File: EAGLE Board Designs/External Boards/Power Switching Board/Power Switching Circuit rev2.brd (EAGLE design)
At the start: 93.6 x 68.1 mm, 64 parts, among them J1 CONNECTOR-3_, J2 CONNECTOR-4_SOURIAU_, J3 CONNECTOR-4_SOURIAU_, K1 J115F11A6*, Q1 TRANSISTOR_N_MOS_2-7K1S_TK100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, Q2 TRANSISTOR_N_MOS_2-7K1S_TK100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, Q3 TRANSISTOR_N_MOS_2-7K1S_TK100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, Q4 TRANSISTOR_N_MOS_2-7K1S_TK100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, U1 LTC4421

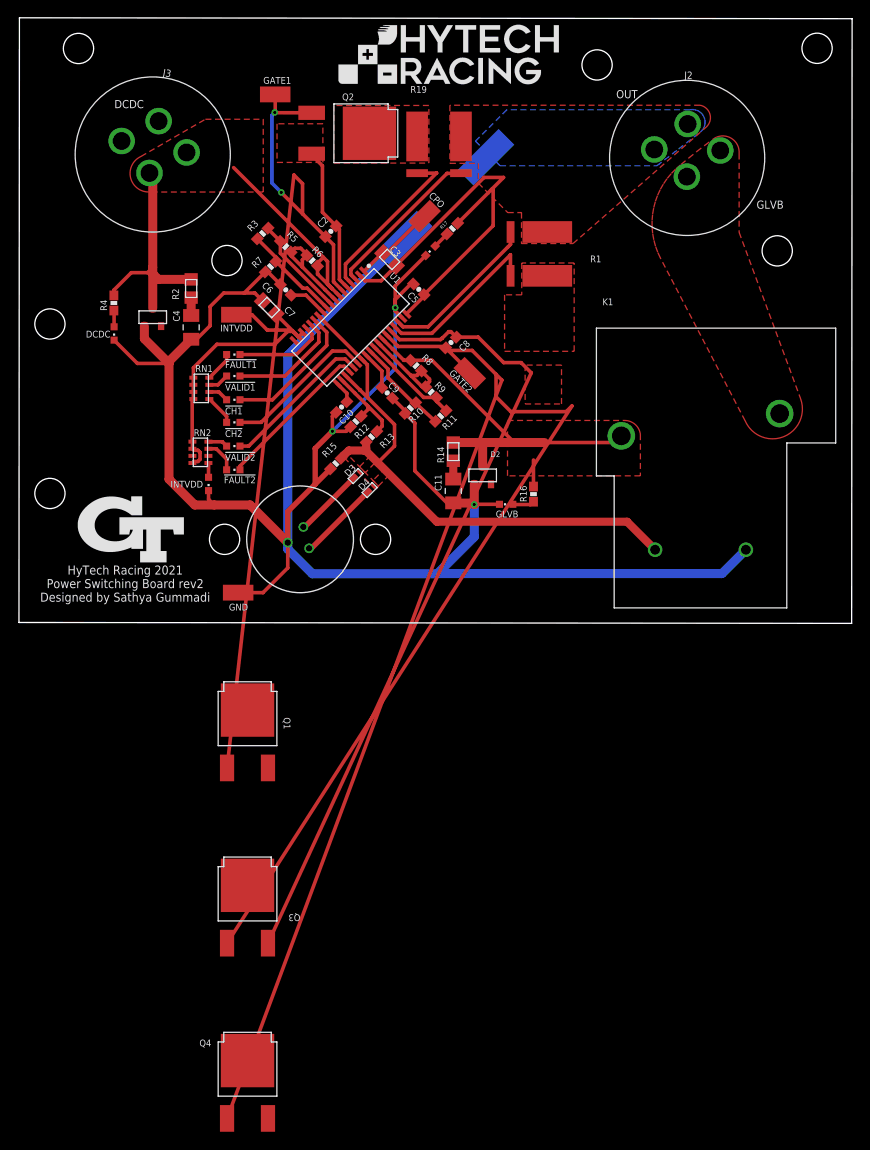
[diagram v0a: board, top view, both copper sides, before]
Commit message: Revert "Replaced mosfets with new device in new library"
This reverts commit 47685a596586f3a57bfaa4732962c561ce9df098.
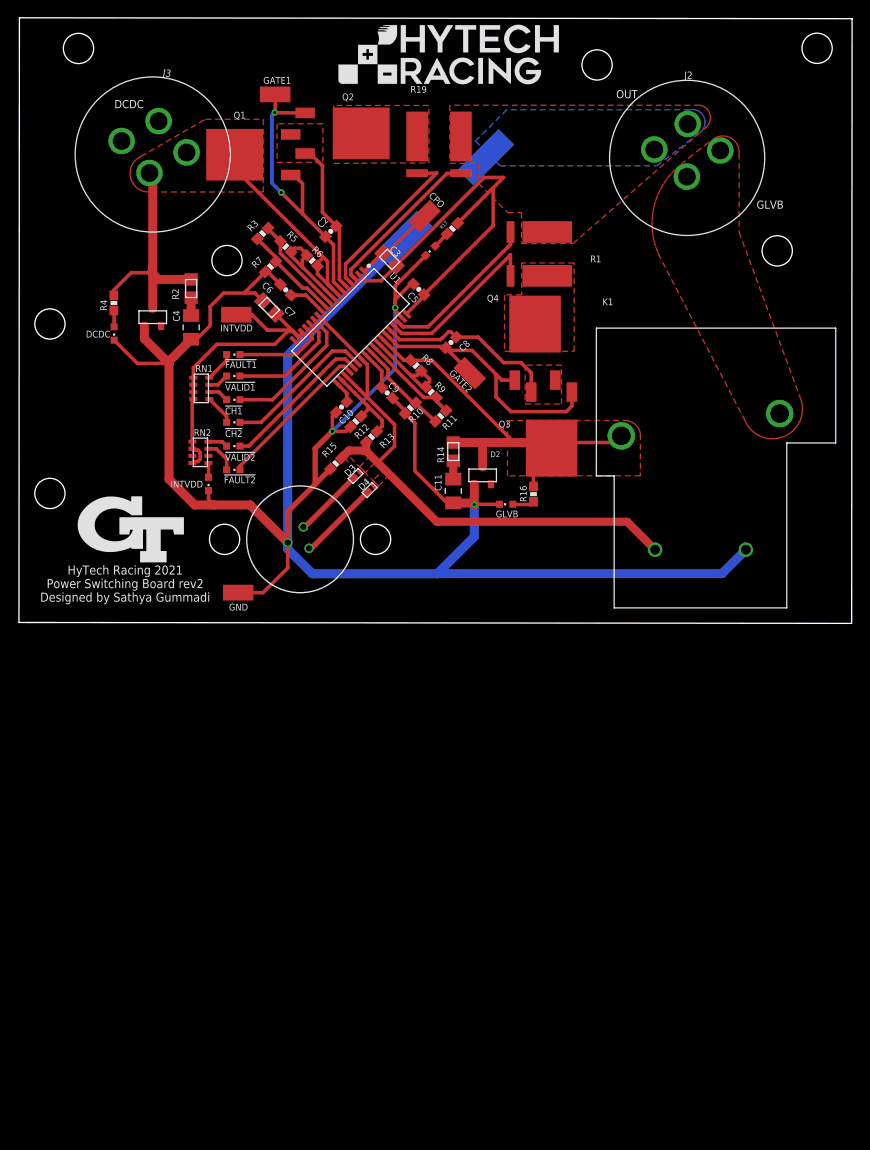
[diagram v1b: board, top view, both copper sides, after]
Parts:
- Q1, Q2, Q3, Q4: value TRANSISTOR_N_MOS_2-7K1S_TK100S04N1L,LQ -> TK100S04N1L; device HyTechDevices:DPAK(2-7K1S) -> HyTechDevices:TO-252-3
- moved Q4 89.7 mm to (30.0, 3.00)
- moved Q1 65.4 mm to (-1.68, 24.1), turned to 90 degrees
- moved Q3 64.1 mm to (31.9, -6.81), turned to 180 degrees
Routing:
- net GATE2: track 191.5 -> 34.2 mm
- net SOURCE2: track 89.2 -> 20.8 mm
- net GATE1: track 101.8 -> 34.4 mm
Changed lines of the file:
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@@
 <attribute name="RESISTANCE" value="0.0013" x="28.1178" y="11.938" size="1.778" layer="27" rot="R180" display="off"/>
 </element>
-<element name="Q1" library="HyTechDevices" package="DPAK(2-7K1S)" value="TRANSISTOR_N_MOS_2-7K1S_TK100S04N1L,LQ" x="-2.3" y="-41.3206" smashed="yes">
-<attribute name="DKPN" value="TK100S04N1LLQ" x="-2.3" y="-41.3206" size="1.778" layer="27" display="off"/>
-<attribute name="MANUFACTURER" value="Toshiba Semiconductor and Storage" x="-2.3" y="-41.3206" size="1.778" layer="27" display="off"/>
-<attribute name="MOPN" value="757-TK100S04N1LLQ" x="-2.3" y="-41.3206" size="1.778" layer="27" display="off"/>
-<attribute name="MPN" value="TK100S04N1L,LQ" x="-2.3" y="-41.3206" size="1.778" layer="27" display="off"/>
-<attribute name="NAME" x="1.764" y="-39.1362" size="0.762" layer="25" ratio="6" rot="SR270"/>
+<element name="Q1" library="HyTechDevices" package="TO-252-3" value="TK100S04N1L" x="-1.6764" y="24.1046" smashed="yes" rot="R90">
+<attribute name="MPN" value="TK100S04N1L,LQ" x="-1.6764" y="24.1046" size="1.778" layer="27" rot="R90" display="off"/>
+<attribute name="NAME" x="-3.8608" y="28.1686" size="0.762" layer="25" ratio="6" rot="SR0"/>
 </element>
-<element name="Q2" library="HyTechDevices" package="DPAK(2-7K1S)" value="TRANSISTOR_N_MOS_2-7K1S_TK100S04N1L,LQ" x="8.4074" y="26.5176" smashed="yes" rot="R270">
-<attribute name="DKPN" value="TK100S04N1LLQ" x="8.4074" y="26.5176" size="1.778" layer="27" rot="R270" display="off"/>
-<attribute name="MANUFACTURER" value="Toshiba Semiconductor and Storage" x="8.4074" y="26.5176" size="1.778" layer="27" rot="R270" display="off"/>
-<attribute name="MOPN" value="757-TK100S04N1LLQ" x="8.4074" y="26.5176" size="1.778" layer="27" rot="R270" display="off"/>
+<element name="Q2" library="HyTechDevices" package="TO-252-3" value="TK100S04N1L" x="8.4074" y="26.5176" smashed="yes" rot="R270">
 <attribute name="MPN" value="TK100S04N1L,LQ" x="8.4074" y="26.5176" size="1.778" layer="27" rot="R270" display="off"/>
 <attribute name="NAME" x="8.3312" y="30.226" size="0.762" layer="25" ratio="6" rot="SR0"/>
 </element>
-<element name="Q4" library="HyTechDevices" package="DPAK(2-7K1S)" value="TRANSISTOR_N_MOS_2-7K1S_TK100S04N1L,LQ" x="-2.3" y="-80.7206" smashed="yes">
-<attribute name="DKPN" value="TK100S04N1LLQ" x="-2.3" y="-80.7206" size="1.778" layer="27" display="off"/>
-<attribute name="MANUFACTURER" value="Toshiba Semiconductor and Storage" x="-2.3" y="-80.7206" size="1.778" layer="27" display="off"/>
-<attribute name="MOPN" value="757-TK100S04N1LLQ" x="-2.3" y="-80.7206" size="1.778" layer="27" display="off"/>
-<attribute name="MPN" value="TK100S04N1L,LQ" x="-2.3" y="-80.7206" size="1.778" layer="27" display="off"/>
-<attribute name="NAME" x="-7.7102" y="-76.1232" size="0.762" layer="25" ratio="6" rot="SR0"/>
+<element name="Q4" library="HyTechDevices" package="TO-252-3" value="TK100S04N1L" x="30.0228" y="2.9972" smashed="yes">
+<attribute name="MPN" value="TK100S04N1L,LQ" x="30.0228" y="2.9972" size="1.778" layer="27" display="off"/>
+<attribute name="NAME" x="24.6126" y="7.5946" size="0.762" layer="25" ratio="6" rot="SR0"/>
 </element>
-<element name="Q3" library="HyTechDevices" package="DPAK(2-7K1S)" value="TRANSISTOR_N_MOS_2-7K1S_TK100S04N1L,LQ" x="-2.3" y="-61.0206" smashed="yes">
-<attribute name="DKPN" value="TK100S04N1LLQ" x="-2.3" y="-61.0206" size="1.778" layer="27" display="off"/>
-<attribute name="MANUFACTURER" value="Toshiba Semiconductor and Storage" x="-2.3" y="-61.0206" size="1.778" layer="27" display="off"/>
-<attribute name="MOPN" value="757-TK100S04N1LLQ" x="-2.3" y="-61.0206" size="1.778" layer="27" display="off"/>
-<attribute name="MPN" value="TK100S04N1L,LQ" x="-2.3" y="-61.0206" size="1.778" layer="27" display="off"/>
-<attribute name="NAME" x="3.6436" y="-61.2746" size="0.762" layer="25" ratio="6" rot="SR180"/>
+<element name="Q3" library="HyTechDevices" package="TO-252-3" value="TK100S04N1L" x="31.877" y="-6.8072" smashed="yes" rot="R180">
+<attribute name="MPN" value="TK100S04N1L,LQ" x="31.877" y="-6.8072" size="1.778" layer="27" rot="R180" display="off"/>
+<attribute name="NAME" x="25.9334" y="-6.5532" size="0.762" layer="25" ratio="6" rot="SR0"/>
 </element>
 <element name="RN2" library="HyTechDevices" package="1206-RES" value="RESISTOR_NETWORK_4_10K" x="-7.5946" y="-9.3472" smashed="yes" rot="R90">
@@
 <wire x1="-17.3228" y1="8.89" x2="-17.3228" y2="8.2922" width="0.4064" layer="1"/>
 <contactref element="Q1" pad="2"/>
-<wire x1="-12.954" y1="6.8453" x2="-2.3" y2="-38.3206" width="0" layer="19" extent="1-1"/>
-<wire x1="-9.14756875" y1="24.361534375" x2="-13.3200875" y2="22.053828125" width="0" layer="19" extent="1-1"/>
-<wire x1="-3.8608" y1="22.6568" x2="-9.14756875" y2="24.361534375" width="0" layer="19" extent="1-1"/>
 </signal>
 <signal name="RIGHT_BRB">
@@
 <contactref element="Q4" pad="1"/>
 <contactref element="Q3" pad="1"/>
-<wire x1="22.9476" y1="2.1082" x2="25.6343" y2="-0.5785" width="0.4064" layer="1"/>
+<wire x1="22.9476" y1="2.1082" x2="25.2279" y2="-0.1721" width="0.4064" layer="1"/>
+<wire x1="25.2279" y1="-0.1721" x2="25.6343" y2="-0.5785" width="0.4064" layer="1"/>
 <wire x1="20.260659375" y1="2.1082" x2="22.9476" y2="2.1082" width="0.4064" layer="1"/>
-<wire x1="34.168053125" y1="-4.135146875" x2="-4.6" y2="-64.5206" width="0.4064" layer="1"/>
+<wire x1="34.168053125" y1="-4.135146875" x2="34.157" y2="-2.5772" width="0.4064" layer="1"/>
 <wire x1="34.168053125" y1="-4.135146875" x2="33.528" y2="-4.7752" width="0.4064" layer="1"/>
 <wire x1="25.6343" y1="-3.1045" x2="25.6343" y2="-0.5785" width="0.4064" layer="1"/>
@@
 <wire x1="27.305" y1="-4.7752" x2="25.6343" y2="-3.1045" width="0.4064" layer="1"/>
 <wire x1="25.6343" y1="-0.5785" x2="26.2886" y2="-1.2328" width="0.4064" layer="1"/>
-<wire x1="26.2886" y1="-1.2328" x2="-4.6" y2="-84.2206" width="0.4064" layer="1"/>
+<wire x1="26.2886" y1="-1.2328" x2="27.7428" y2="-1.2328" width="0.4064" layer="1"/>
 </signal>
 <signal name="SOURCE2">
@@
 <wire x1="26.4922" y1="0.7366" x2="28.448" y2="0.7366" width="0.4064" layer="1"/>
 <wire x1="28.448" y1="0.7366" x2="29.597" y2="-0.4124" width="0.4064" layer="1"/>
-<wire x1="29.597" y1="-0.4124" x2="0" y2="-64.5206" width="0.4064" layer="1"/>
+<wire x1="29.597" y1="-0.4124" x2="29.597" y2="-2.5772" width="0.4064" layer="1"/>
 <wire x1="21.17439375" y1="3.598634375" x2="23.630165625" y2="3.598634375" width="0.4064" layer="1"/>
-<wire x1="0" y1="-64.5206" x2="0" y2="-84.2206" width="0" layer="19" extent="1-1"/>
 </signal>
 <signal name="CPO">
@@
 <wire x1="38.9642" y1="-8.246" x2="31.0816" y2="-8.246" width="0.4064" layer="1"/>
 <contactref element="Q3" pad="2"/>
-<wire x1="24.13" y1="-10.9347" x2="-2.3" y2="-58.0206" width="0" layer="19" extent="1-1"/>
-<wire x1="27.305" y1="-7.874" x2="24.13" y2="-10.9347" width="0" layer="19" extent="1-1"/>
-<wire x1="29.845" y1="-10.2108" x2="27.305" y2="-7.874" width="0" layer="19" extent="1-1"/>
 </signal>
 <signal name="GATE1">
@@
 <contactref element="Q2" pad="1"/>
 <wire x1="0.762" y1="28.8544" x2="0.7898125" y2="28.8265875" width="0.4064" layer="1"/>
-<wire x1="0.7898125" y1="28.8265875" x2="4.9074" y2="28.8176" width="0.4064" layer="1"/>
+<wire x1="0.7898125" y1="28.8265875" x2="4.1774" y2="28.7976" width="0.4064" layer="1"/>
 <wire x1="3.8862" y1="20.8534" x2="3.8862" y2="17.4666625" width="0.4064" layer="1"/>
 <wire x1="6.23143125" y1="15.12143125" x2="3.8862" y2="17.4666625" width="0.4064" layer="1"/>
@@
 <wire x1="1.4986" y1="19.8628" x2="0.4318" y2="20.9296" width="0.4064" layer="16"/>
 <wire x1="0.4318" y1="20.9296" x2="0.4318" y2="28.5242" width="0.4064" layer="16"/>
-<wire x1="-4.6" y1="-44.8206" x2="2.915" y2="21.8246" width="0.4064" layer="1"/>
+<wire x1="2.5536" y1="21.8246" x2="2.915" y2="21.8246" width="0.4064" layer="1"/>
 <wire x1="2.915" y1="21.8246" x2="3.8862" y2="20.8534" width="0.4064" layer="1"/>
 </signal>
@@
 <contactref element="Q2" pad="3"/>
 <wire x1="6.1214" y1="22.86" x2="4.7438" y2="24.2376" width="0.4064" layer="1"/>
-<wire x1="4.7438" y1="24.2376" x2="4.9074" y2="24.2176" width="0.4064" layer="1"/>
-<wire x1="8.9528" y1="9.153771875" x2="0" y2="-44.8206" width="0" layer="19" extent="1-1"/>
+<wire x1="4.7438" y1="24.2376" x2="4.1774" y2="24.2376" width="0.4064" layer="1"/>
 </signal>
 <signal name="!SHDN!">
@@
 </polygon>
 <contactref element="Q4" pad="2"/>
-<wire x1="31.3944" y1="10.4902" x2="-2.3" y2="-77.7206" width="0" layer="19" extent="1-1"/>
 </signal>
 <signal name="OUT2">
@@
 </signal>
 <signal name="N$8">
+<contactref element="R19" pad="2"/>
 <polygon width="0.2032" layer="1" orphans="yes" thermals="no">
 <vertex x="18.0848" y="23.1648"/>
@@
 </polygon>
 <contactref element="Q2" pad="2"/>
-<contactref element="R19" pad="2"/>
-<wire x1="11.4074" y1="26.5176" x2="16.764" y2="26.162" width="0" layer="19" extent="1-1"/>
 </signal>
 <signal name="N$6">
